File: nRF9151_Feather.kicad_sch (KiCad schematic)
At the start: 10 parts

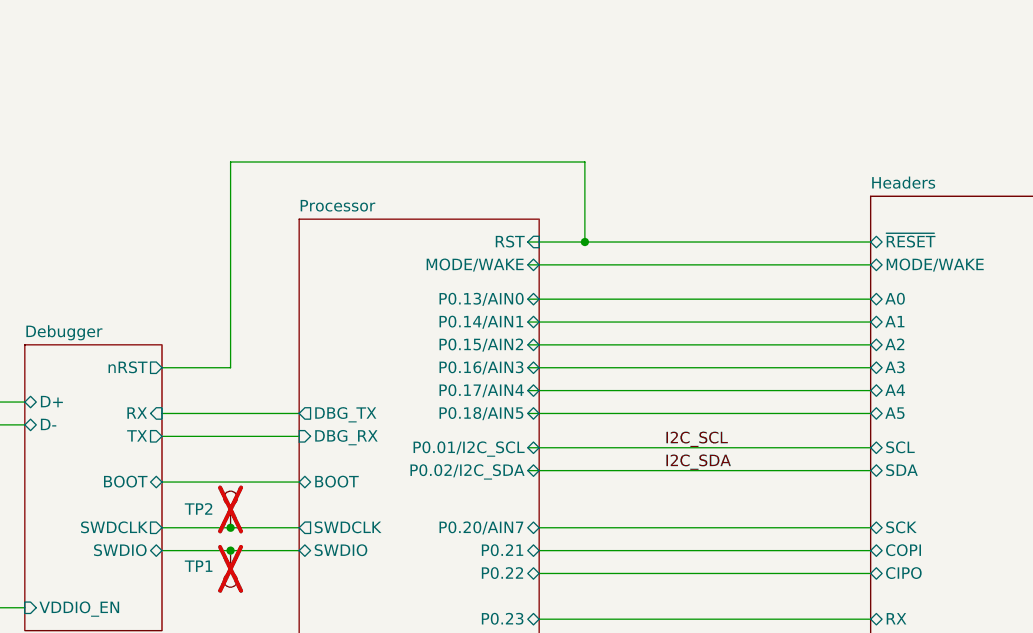
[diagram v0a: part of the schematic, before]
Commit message: Fixing error in schematic w/ nRST
nRST on debugger should not (and is not) connected to the nRST signal to the processor. Cleaning up schematic to clear up confusion around that. PCB routing remains unchanged.
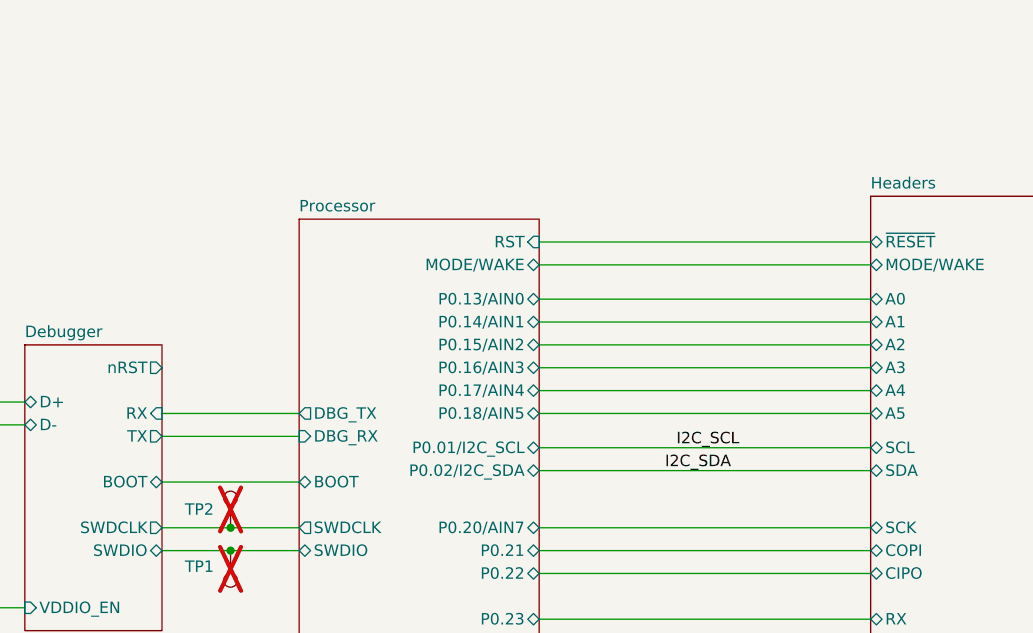
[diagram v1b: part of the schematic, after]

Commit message: Adding variant control
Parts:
- TP1, TP2: now left out of the parts list
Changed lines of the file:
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@@
 		(unit 1)
 		(exclude_from_sim no)
-		(in_bom yes)
+		(in_bom no)
 		(on_board yes)
 		(dnp yes)
@@
 		(unit 1)
 		(exclude_from_sim no)
-		(in_bom yes)
+		(in_bom no)
 		(on_board yes)
 		(dnp yes)
